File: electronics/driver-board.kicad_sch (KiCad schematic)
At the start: 52 parts, among them J2 Conn_01x05_Socket, J3 S4B-XH-A, J4 Qwiic_RA, J5 Conn_01x06_Female, J6 Conn_01x05_Socket, J7 Conn_01x02, J8 Conn_01x08_Socket, J9 Conn_01x01_Socket, SW1 SW_Push, SW2 SW_Push, SW3 SW_Push, SW4 SW_Push, U1 LMR16006YQ3, U3 ESP32-C6-MINI-1/U, U5 TMC5240-TSSOP38, U7 AS5047D

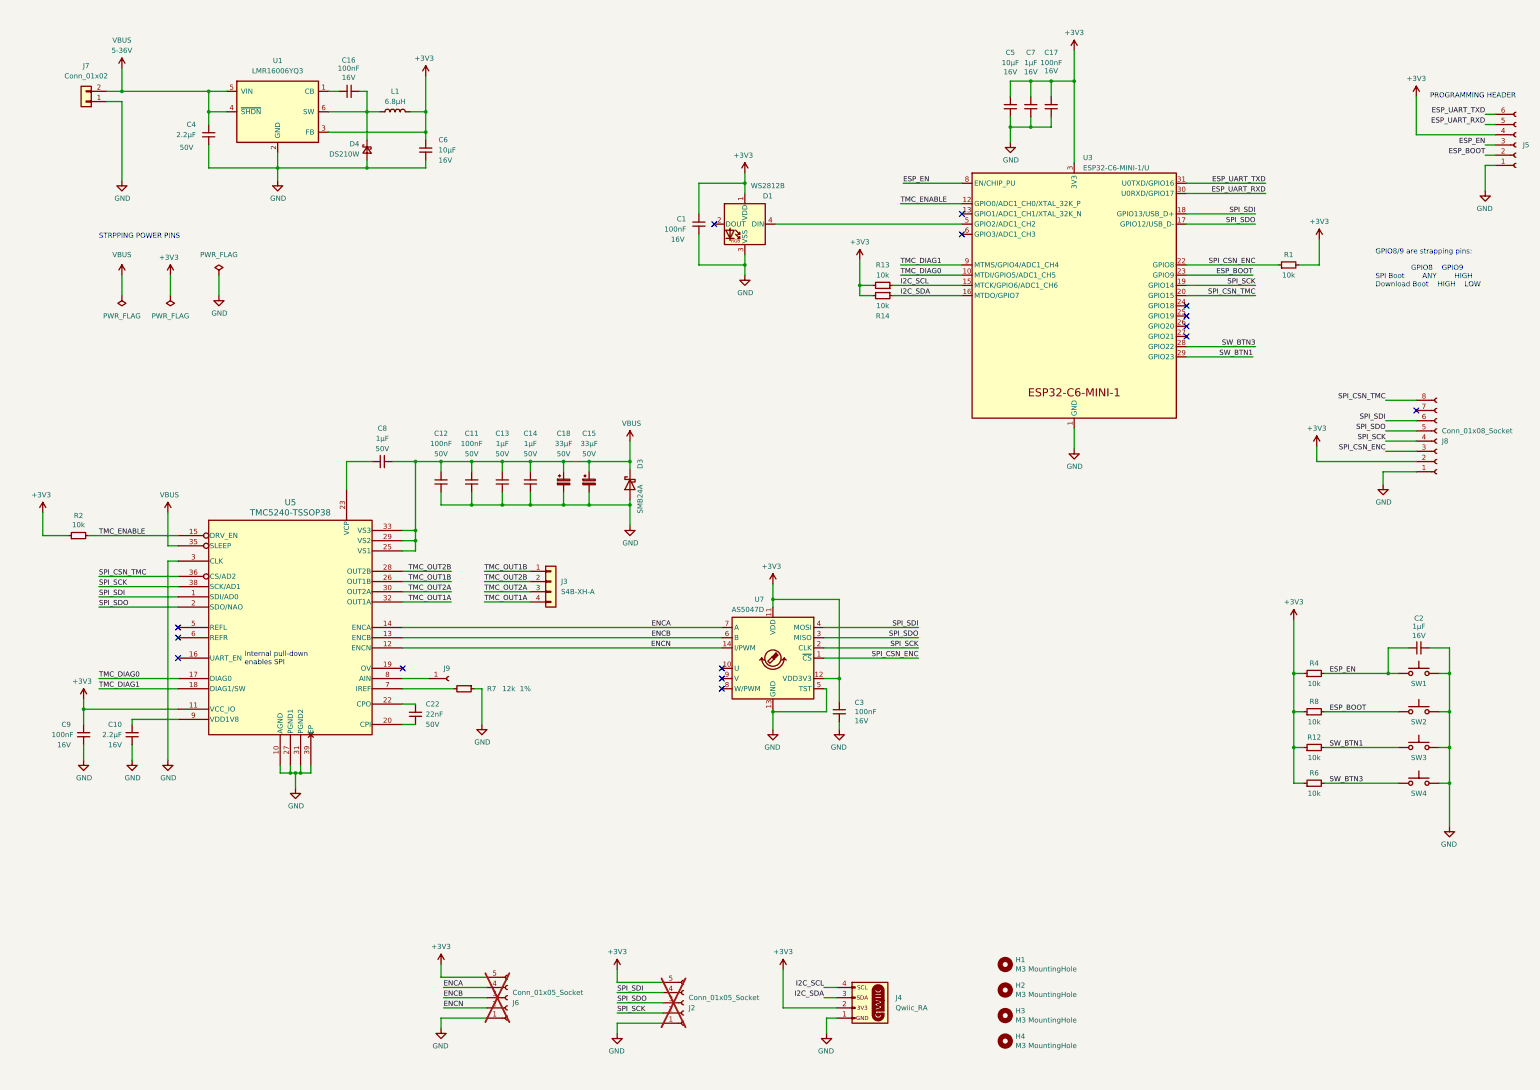
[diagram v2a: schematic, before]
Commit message: incorporated USB port and refined board layout wip
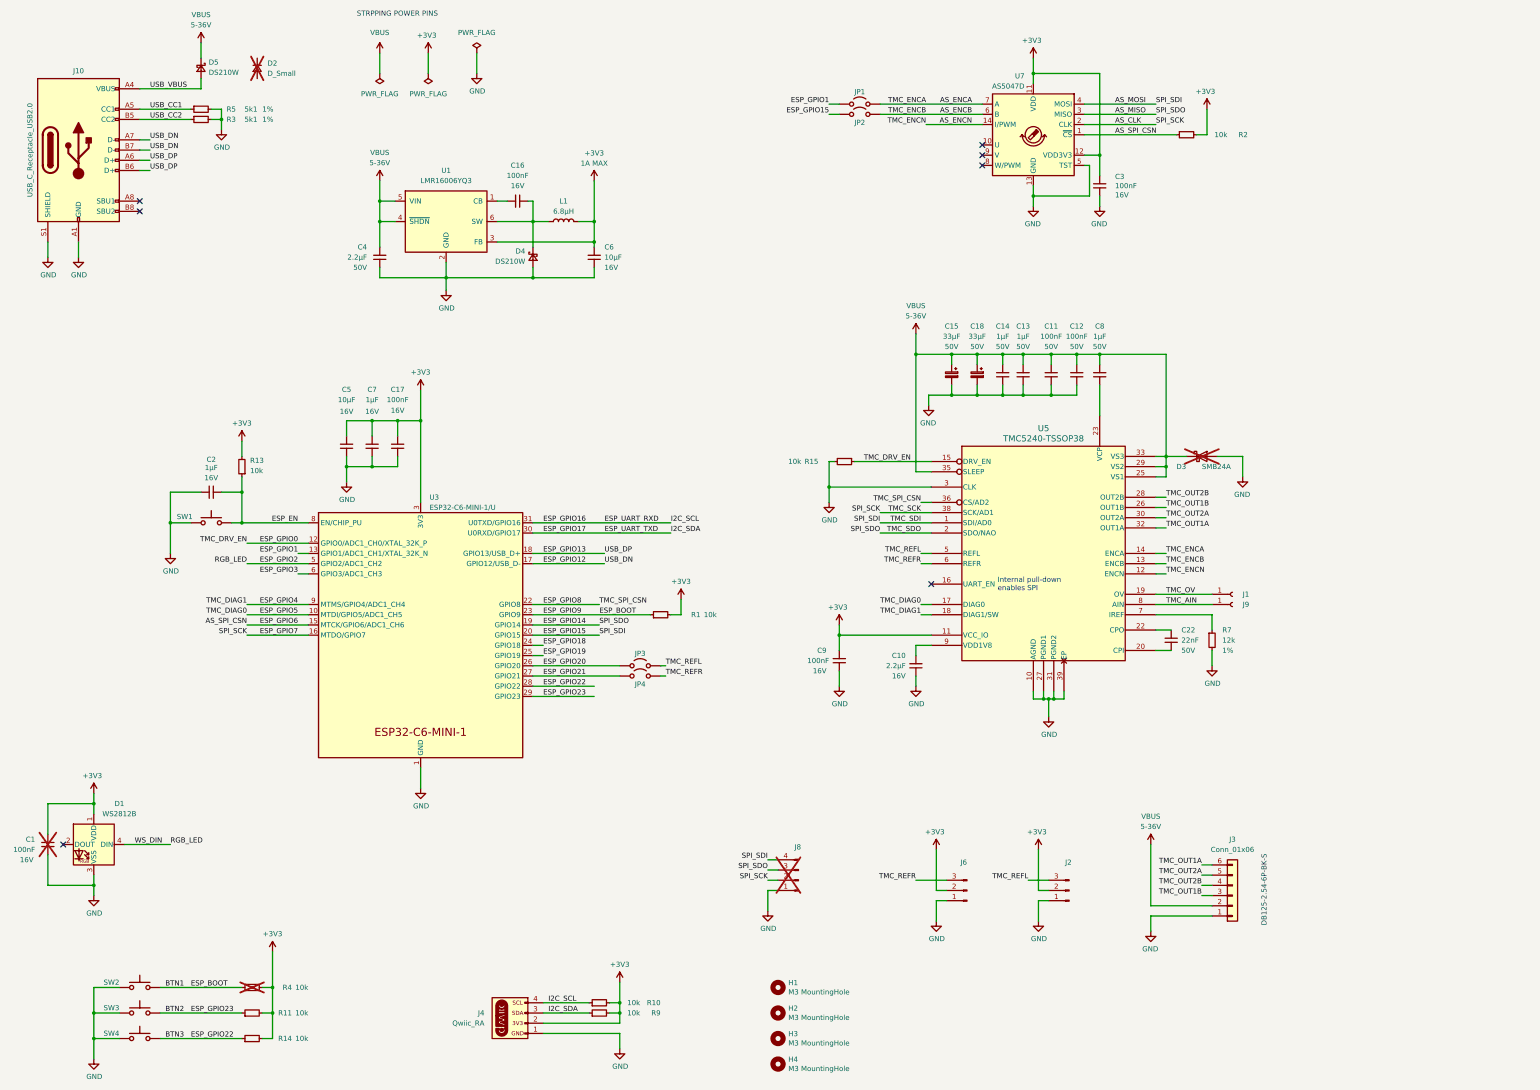
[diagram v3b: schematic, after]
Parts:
- removed J2, J6: Conn_01x05_Socket, Connector_PinHeader_2.54mm:PinHeader_1x05_P2.54mm_Vertical, symbol Connector:Conn_01x05_Socket
- removed J3: S4B-XH-A, Connector_JST:JST_XH_S4B-XH-A-1_1x04_P2.50mm_Horizontal, symbol Connector_Generic:Conn_01x04
- removed J5: Conn_01x06_Female, Connector_PinSocket_1.27mm:PinSocket_1x06_P1.27mm_Vertical, symbol Connector:Conn_01x06_Female
- removed J7: Conn_01x02, Connector_JST:JST_XH_B2B-XH-A_1x02_P2.50mm_Vertical, symbol Connector_Generic:Conn_01x02
- removed J8: Conn_01x08_Socket, Connector_PinHeader_2.54mm:PinHeader_2x04_P2.54mm_Vertical, symbol Connector:Conn_01x08_Socket
- removed R12, R6, R8: 10k, Resistor_SMD:R_0603_1608Metric, symbol Device:R_Small
- added D2: D_Small, symbol Device:D_Small
- added D5: DS210W, Diode_SMD:D_SOD-123F, symbol Device:D_Schottky_Small
- added J1: Conn_01x01_Socket, TestPoint:TestPoint_Pad_D2.0mm, symbol Connector:Conn_01x01_Socket
- added J10: USB_C_Receptacle_USB2.0, Connector_USB:USB_C_Receptacle_GCT_USB4105-xx-A_16P_TopMnt_Horizontal, symbol Connector:USB_C_Receptacle_USB2.0
- added J2, J6: Conn_01x03_Pin, Connector_PinHeader_2.54mm:PinHeader_1x03_P2.54mm_Vertical, symbol Connector:Conn_01x03_Pin
- added J3: Conn_01x06, TerminalBlock_Phoenix:TerminalBlock_Phoenix_MPT-0,5-6-2.54_1x06_P2.54mm_Horizontal, symbol SparkFun-Connector:Conn_01x06
- added J8: Conn_01x04_Pin, Connector_PinHeader_2.54mm:PinHeader_1x04_P2.54mm_Vertical, symbol Connector:Conn_01x04_Pin
- added JP1, JP2, JP3, JP4: Jumper_2_Open, Jumper:SolderJumper-2_P1.3mm_Open_Pad1.0x1.5mm, symbol Jumper:Jumper_2_Open
- added R10, R11, R15, R9: 10k, Resistor_SMD:R_0603_1608Metric, symbol Device:R_Small
- added R3, R5: 5k1, Resistor_SMD:R_0603_1608Metric, symbol Device:R_Small
- C1, D3, R4: now not fitted; now left out of the parts list
- D1: footprint LED_SMD:LED_SK6812MINI_PLCC4_3.5x3.5mm_P1.75mm -> LED_SMD:LED_SK6812_EC15_1.5x1.5mm; LCSC C527089 -> (none); Manf Worldsemi -> (none); Manf# WS2812B-Mini -> (none)
- J4: footprint SparkFun-Connector:JST04_1MM_RA -> SparkFun-Connector:JST04_1MM_Vertical
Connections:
- net +3V3: now also R2.2, R4.2, J2.2 (Pin_2), J6.2 (Pin_2), R10.2, R11.2, R9.2; no longer R2.1, R4.1
- net ESP_EN: now also R13.1; no longer R4.2
- net GND: now also R7.2, J10.A1 (GND), J10.A12 (GND), J10.B1 (GND), J10.B12 (GND), J10.S1 (SHIELD), J2.1 (Pin_1), J3.1 (Pin_1), J6.1 (Pin_1), J8.1 (Pin_1), R15.2, R3.2, R5.2; no longer R7.1
- net TMC_OUT1A: now also J3.6 (Pin_6)
- net TMC_OUT1B: now also J3.3 (Pin_3)
- net TMC_OUT2A: now also J3.5 (Pin_5)
- net TMC_OUT2B: now also J3.4 (Pin_4)
- net VBUS: now also C8.1, D5.1 (K), J3.2 (Pin_2); no longer C8.2
- net ESP_GPIO2: now reaches D1.4 (DIN), U3.5 (GPIO2/ADC1_CH2)
- net TMC_AIN: now reaches J9.1 (Pin_1), U5.8 (AIN)
- net at U5.7 (IREF): now also R7.1; no longer R7.2
- net at U5.23 (VCP): now also C8.2; no longer C8.1
- net ESP_GPIO1: now reaches U3.13 (GPIO1/ADC1_CH1/XTAL_32K_N)
- net ESP_GPIO1: now also JP1.2 (B)
- net ESP_GPIO18: now reaches U3.24 (GPIO18)
- net ESP_GPIO19: now reaches U3.25 (GPIO19)
- net ESP_GPIO20: now reaches U3.26 (GPIO20)
- net ESP_GPIO20: now also JP3.1 (A)
- net ESP_GPIO21: now reaches U3.27 (GPIO21)
- net ESP_GPIO21: now also JP4.2 (B)
- net ESP_GPIO3: now reaches U3.6 (GPIO3/ADC1_CH3)
- net TMC_OV: now reaches U5.19 (OV)
- net TMC_OV: now also J1.1 (Pin_1)
- net TMC_REFL: now reaches U5.5 (REFL)
- net TMC_REFL: now also J2.3 (Pin_3), JP3.2 (B)
- net TMC_REFR: now reaches U5.6 (REFR)
- net TMC_REFR: now also J6.3 (Pin_3), JP4.1 (A)
- net ENCA renamed AS_ENCA
- net AS_ENCA: now also JP1.1 (A)
- net ENCB renamed AS_ENCB
- net AS_ENCB: now also JP2.1 (A)
- net ENCN renamed AS_ENCN
- net ESP_BOOT renamed BTN1
- net BTN1: now also R1.1, R4.1
- net ESP_UART_RXD renamed ESP_GPIO17
- net ESP_GPIO17: now also J4.3 (Pin_3), R9.1
- net ESP_UART_TXD renamed ESP_GPIO16
- net ESP_GPIO16: now also J4.4 (Pin_4), R10.1
- removed net I2C_SCL: J4.4 (Pin_4), R13.1, U3.15 (MTCK/GPIO6/ADC1_CH6)
- removed net I2C_SDA: J4.3 (Pin_3), R14.1, U3.16 (MTDO/GPIO7)
- removed net SPI_CSN_ENC: R1.1, U3.22 (GPIO8), U7.1 (~{CS})
- net SPI_CSN_TMC renamed AS_MOSI
- net AS_MOSI: now also U5.1 (SDI/AD0), U7.4 (MOSI), J8.4 (Pin_4), JP2.2 (B); no longer U5.36 (CS/AD2)
- net SPI_SCK renamed AS_CLK
- net AS_CLK: now also U3.16 (MTDO/GPIO7), J8.2 (Pin_2); no longer U3.19 (GPIO14)
- removed net SPI_SDI: U3.18 (GPIO13/USB_D+), U5.1 (SDI/AD0), U7.4 (MOSI)
- net SPI_SDO renamed AS_MISO
- net AS_MISO: now also U3.19 (GPIO14), J8.3 (Pin_3); no longer U3.17 (GPIO12/USB_D-)
- net SW_BTN1 renamed BTN2
- net BTN2: now also R11.1
- net SW_BTN3 renamed BTN3
- net BTN3: now also R14.1
- net TMC_DIAG0 renamed ESP_GPIO5
- net TMC_DIAG1 renamed ESP_GPIO4
- net TMC_ENABLE renamed ESP_GPIO0
- net ESP_GPIO0: now also R15.1; no longer R2.2
- new net AS_SPI_CSN: R2.1, U3.15 (MTCK/GPIO6/ADC1_CH6), U7.1 (~{CS})
- new net ESP_GPIO12: J10.A7 (D-), J10.B7 (D-), U3.17 (GPIO12/USB_D-)
- new net ESP_GPIO13: J10.A6 (D+), J10.B6 (D+), U3.18 (GPIO13/USB_D+)
- new net ESP_GPIO8: U3.22 (GPIO8), U5.36 (CS/AD2)
- new net USB_CC1: J10.A5 (CC1), R5.1
- new net USB_CC2: J10.B5 (CC2), R3.1
- new net USB_VBUS: D5.2 (A), J10.A4 (VBUS), J10.A9 (VBUS), J10.B4 (VBUS), J10.B9 (VBUS)
- no-connect marks 15 -> 7
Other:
- note added: "DB125-2.54-6P-BK-S"
- note removed: "GPIO8/9 are strapping pins: GPIO8 GPIO9 SPI Boot ANY HIGH Download Boot HIGH LOW"
- note removed: "PROGRAMMING HEADER"
- moved on the sheet: C10, C11, C12, C13, C14, C15, C16, C17, C18, C2, C22, C3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
